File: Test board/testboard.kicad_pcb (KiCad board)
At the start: 2 copper layers, 39.2 x 62.9 mm, 30 parts, among them IC1 ATMEGA32U4, J1 USBMINI_B05, P1 CONN_1, P2 CONN_1, P3 CONN_1, P4 CONN_1, P5 CONN_1, P6 CONN_1, SW0:0 F0, SW0:1 CTRL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

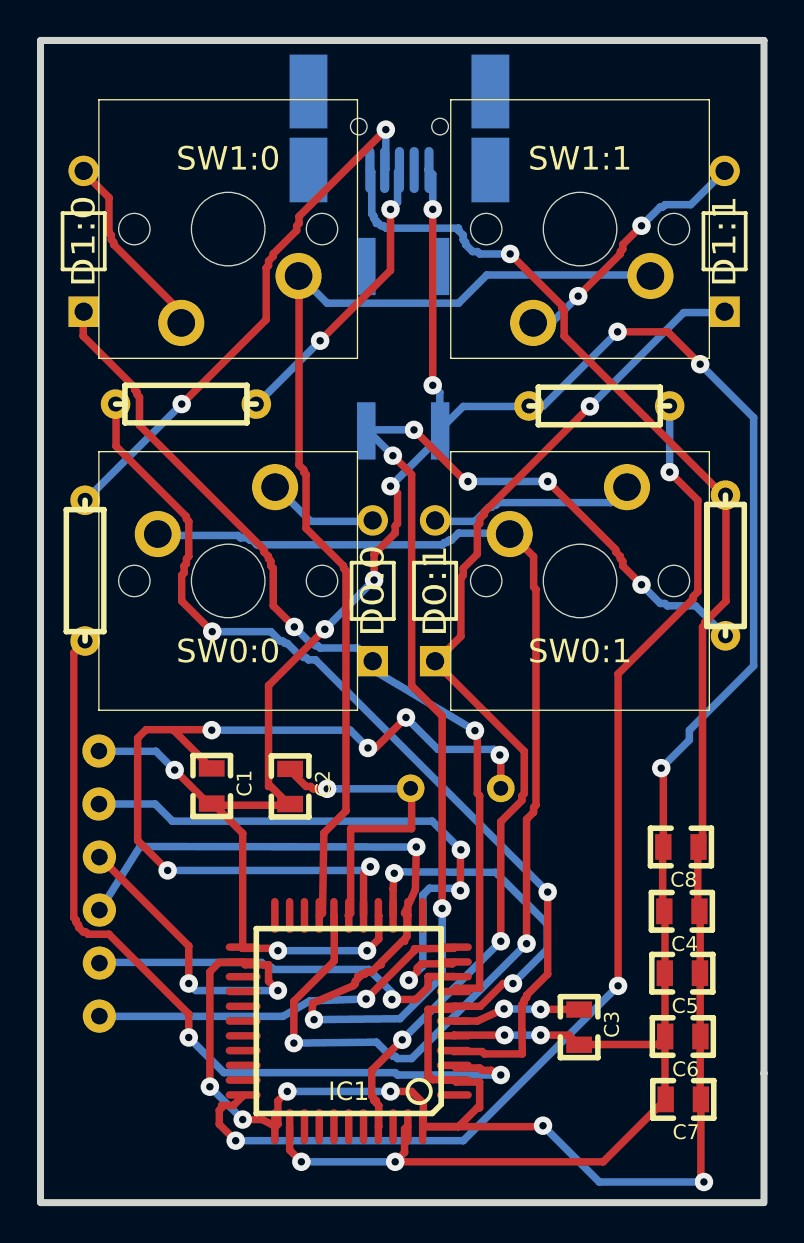
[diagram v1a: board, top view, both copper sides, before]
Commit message: thinner cut line, moved in cut line, pdf printing files
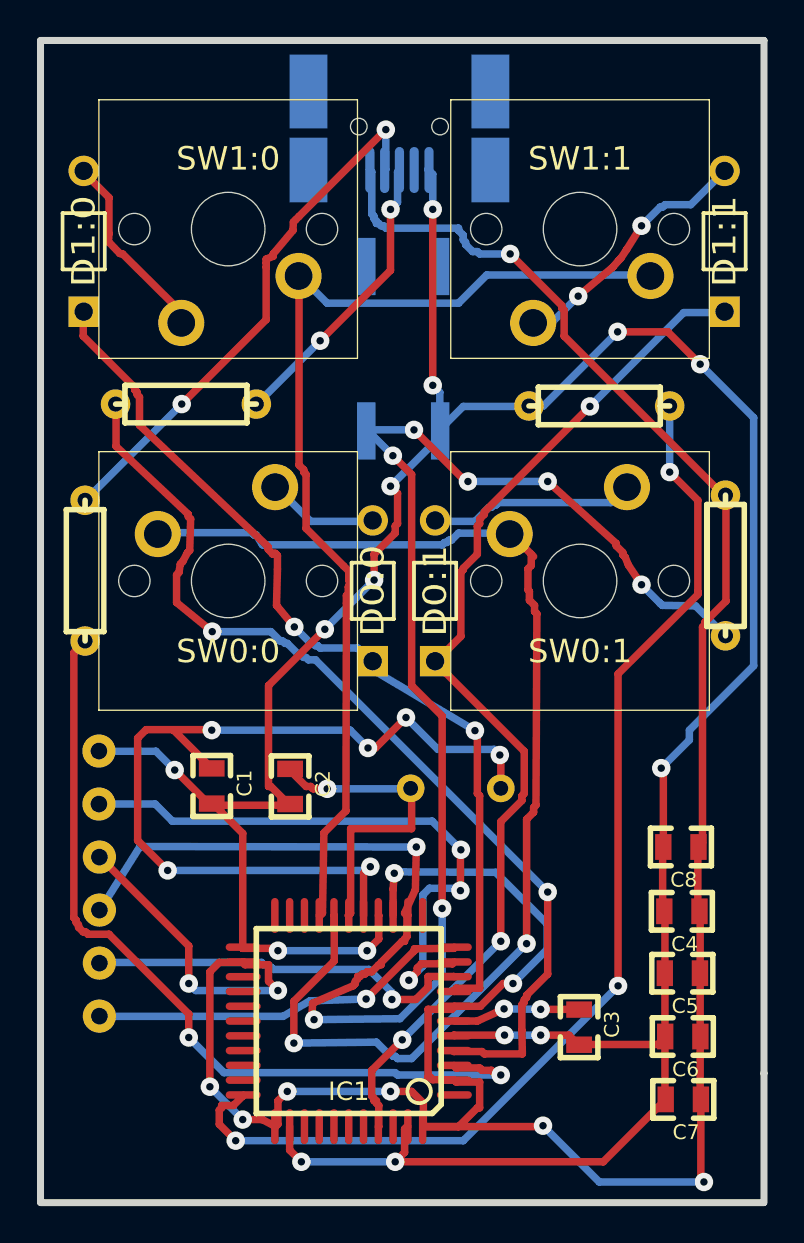
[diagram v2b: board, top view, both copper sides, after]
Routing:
- net /ROW0: track 66.1 -> 66.8 mm

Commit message: change resistor footprints to 0805R, add caps led
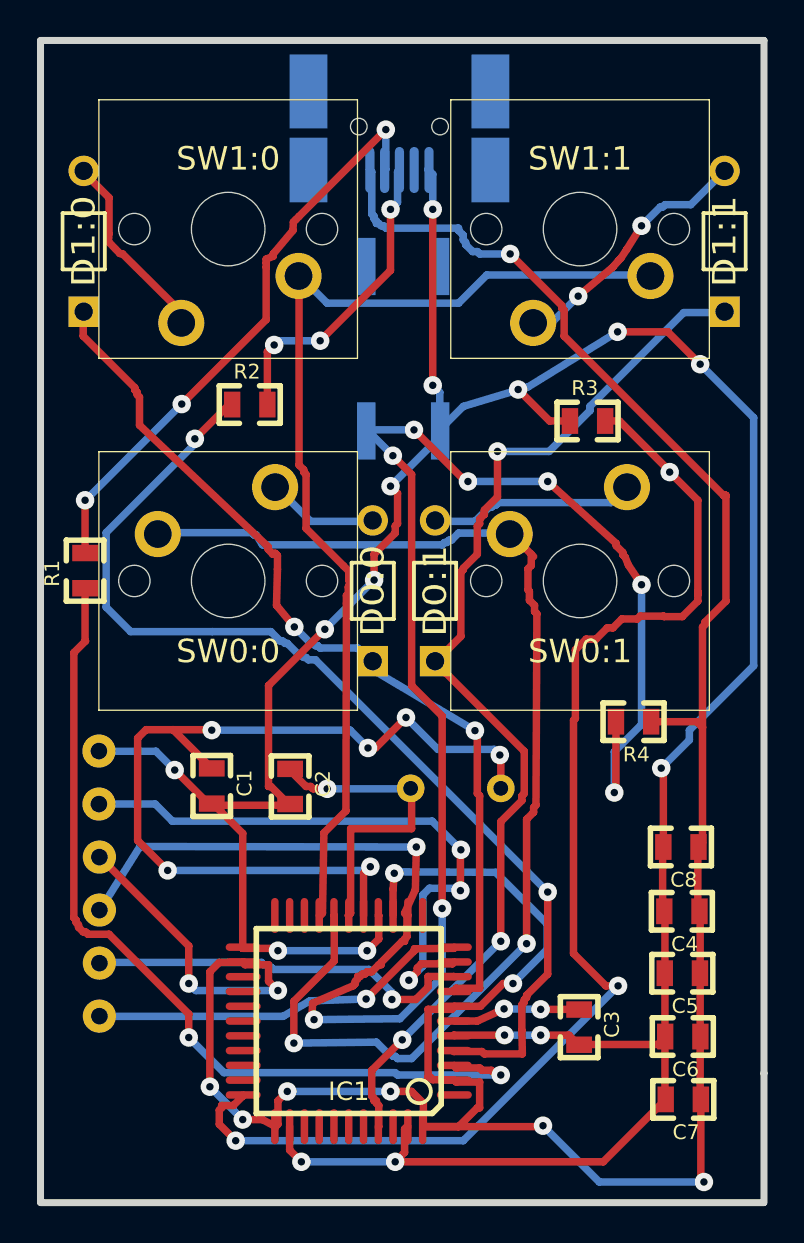
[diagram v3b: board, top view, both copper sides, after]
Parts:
- R1, R2, R3, R4: footprint res:resistor -> 0805:0805R
- moved R4 9.81 mm to (236.9, 179.5), turned to 180 degrees
- moved R2 3.45 mm to (216.2, 162.3)
- moved R3 1.03 mm to (234.4, 163.2)
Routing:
- net /RES: track 95.6 -> 105.6 mm, vias 8 -> 9
- net Net-(IC1-Pad33): track 61.7 -> 67.7 mm
- net Net-(IC1-Pad4): track 52.4 -> 57.3 mm
- net VCC: track 157.4 -> 160.3 mm
- net Net-(IC1-Pad3): track 45.6 -> 48.4 mm
- net Net-(J1-Pad2): track 29.1 -> 31.9 mm, vias 2 -> 3
- net GND: track 167.2 -> 170.0 mm, vias 15 -> 16
- net /COL1: track 57.7 -> 59.4 mm
- net Net-(J1-Pad3): track 16.0 -> 17.1 mm, vias 2 -> 3
